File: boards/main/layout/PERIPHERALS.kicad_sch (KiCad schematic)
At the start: 42 parts, among them Q1 AO3400A, Q7 AO3401A, SW1 DSHP04TJGER, SW2 GT-TC048B-H025-L1, SW3 GT-TC048B-H025-L1, SW5 GT-TC048B-H025-L1, U2 GT-USB-7010ASV, U6 USBLC6-2SC6, U7 TLV7041DBVR

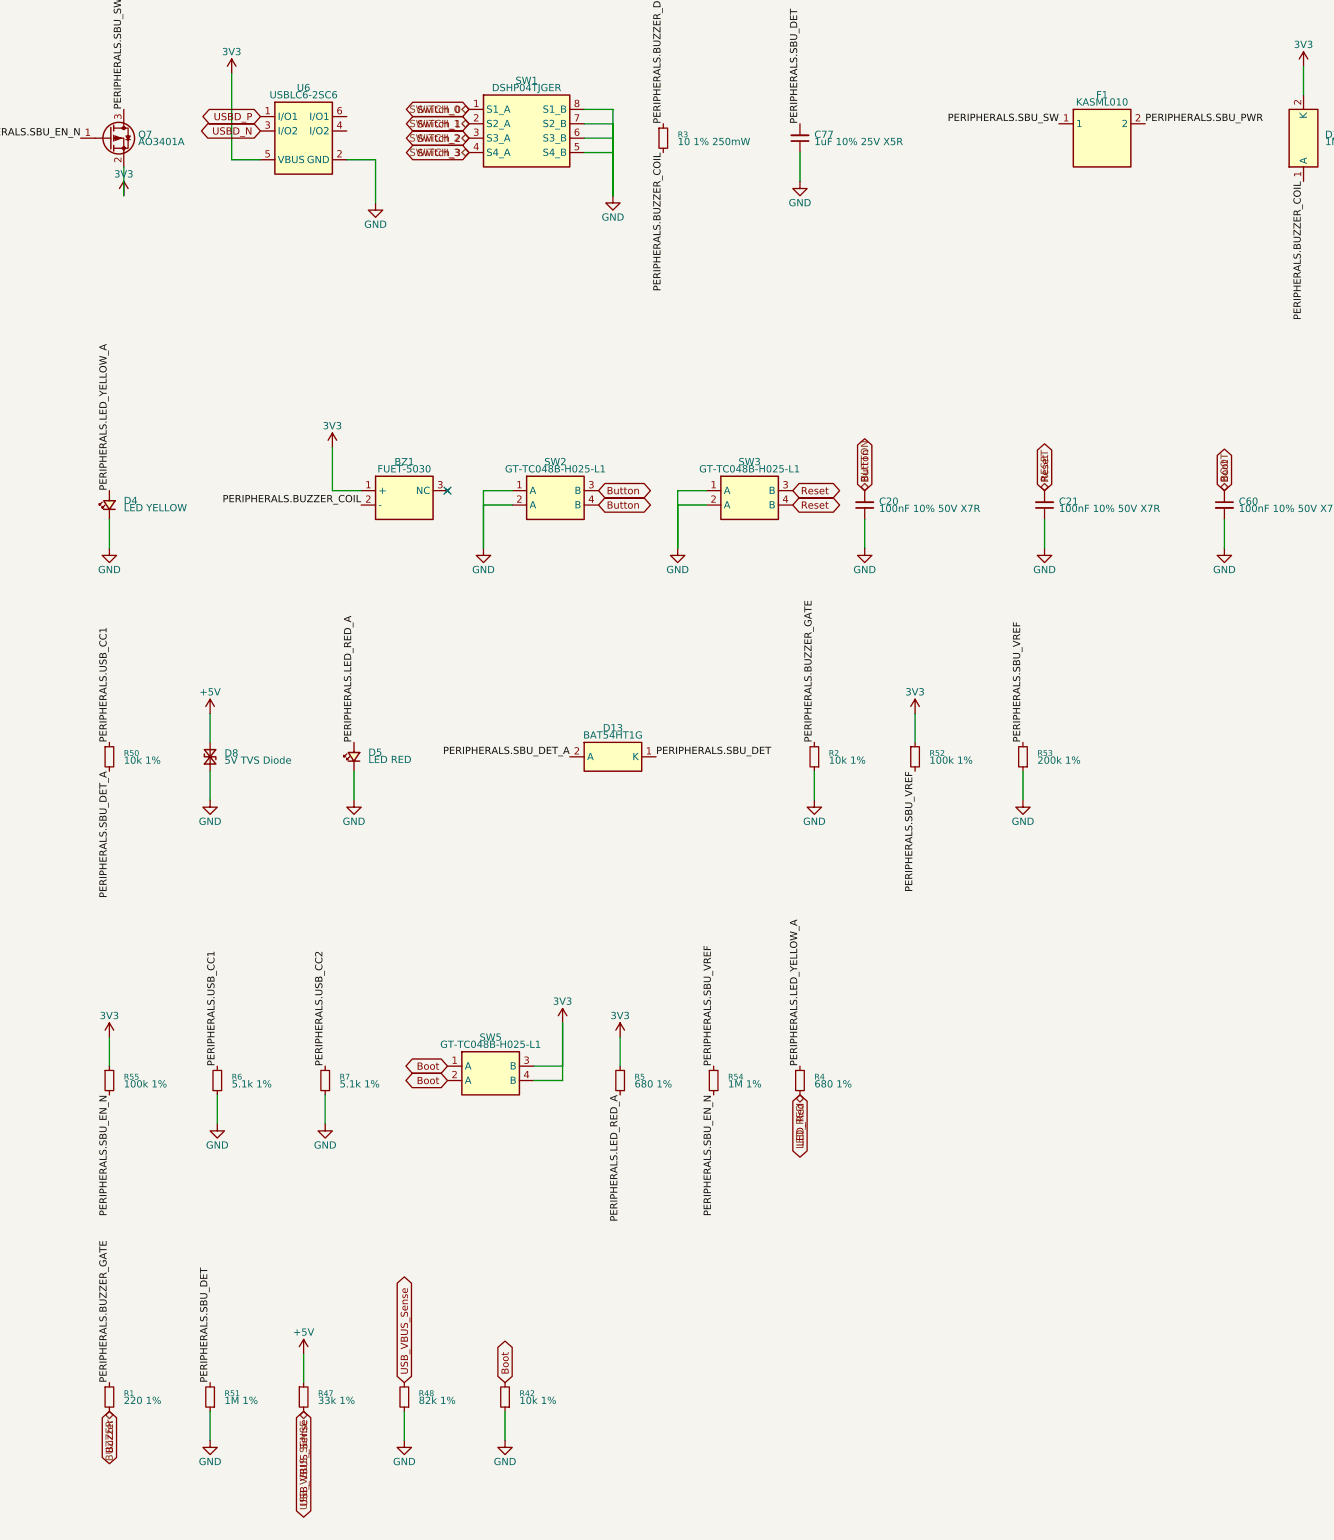
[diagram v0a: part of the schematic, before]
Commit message: 🏷️ Name the main board's module ports after their nets
A sheet pin and its hierarchical label take the module's port name and the root's label the net
name; KiCad's ERC flagged the 33 nets whose two names differed only in case (similar_labels).
GND_BAT becomes a ground port of REGULATORS, so the root shows a power symbol at its sheet pin
instead of a label nothing else joined (label_dangling).
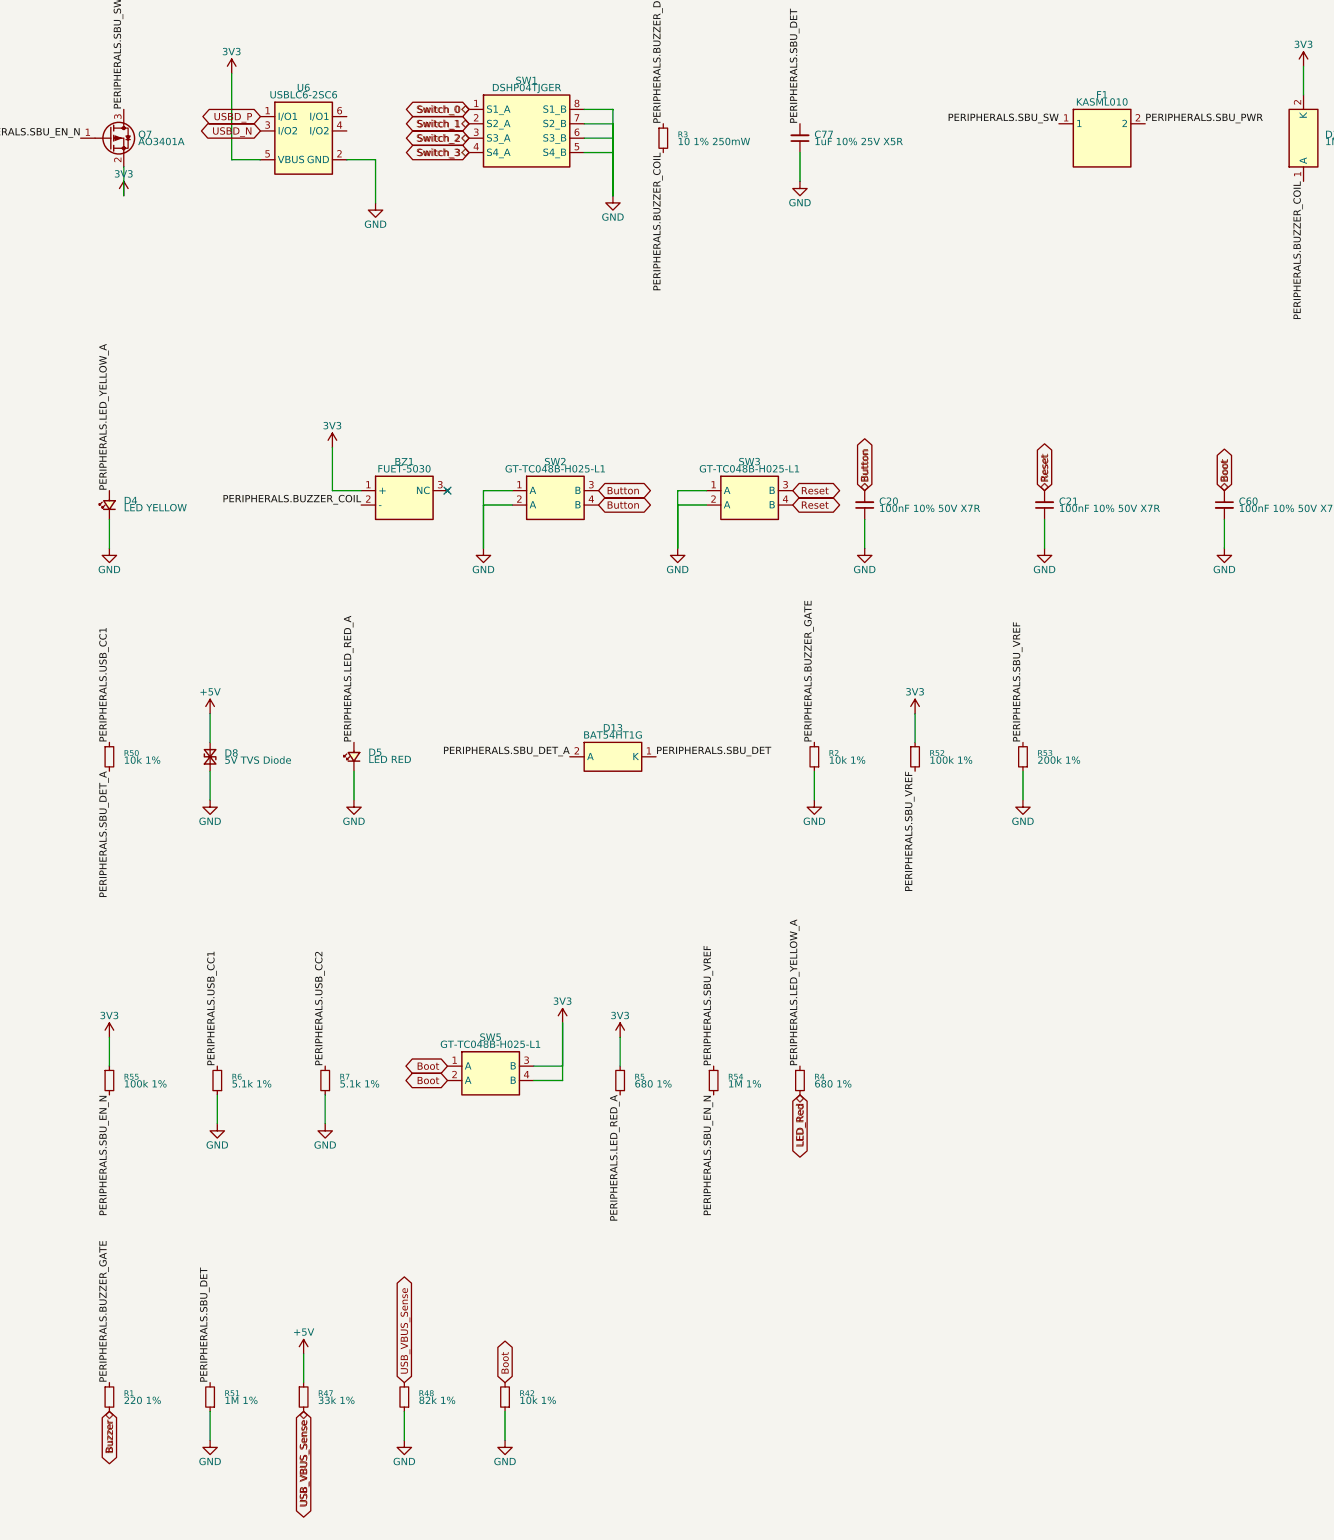
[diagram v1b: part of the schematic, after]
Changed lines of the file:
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@@
 		)
 	)
-	(hierarchical_label "SWITCH_0"
+	(hierarchical_label "USB_VBUS_Sense"
 		(shape bidirectional)
-		(at 181.61 132.08 180)
+		(at 152.4 361.95 270)
 		(effects
 			(font
@@
 		)
 	)
+	(hierarchical_label "Boot"
+		(shape bidirectional)
+		(at 314.96 199.39 90)
+		(effects
+			(font
+				(size 1.27 1.27)
+			)
+			(justify left)
+		)
+	)
+	(hierarchical_label "Switch_0"
+		(shape bidirectional)
+		(at 181.61 132.08 180)
+		(effects
+			(font
+				(size 1.27 1.27)
+			)
+			(justify right)
+		)
+	)
 	(hierarchical_label "LED_ARGB"
 		(shape bidirectional)
@@
 		)
 	)
-	(hierarchical_label "BOOT"
+	(hierarchical_label "Switch_2"
 		(shape bidirectional)
-		(at 314.96 199.39 90)
-		(effects
-			(font
-				(size 1.27 1.27)
-			)
-			(justify left)
-		)
-	)
-	(hierarchical_label "BUZZER"
-		(shape bidirectional)
-		(at 118.11 361.95 270)
+		(at 181.61 137.16 180)
 		(effects
 			(font
@@
 		)
 	)
-	(hierarchical_label "LED_RED"
+	(hierarchical_label "Switch_3"
 		(shape bidirectional)
-		(at 240.03 306.07 270)
+		(at 181.61 139.7 180)
 		(effects
 			(font
@@
 		)
 	)
-	(hierarchical_label "BUTTON"
+	(hierarchical_label "Reset"
 		(shape bidirectional)
-		(at 251.46 199.39 90)
+		(at 283.21 199.39 90)
 		(effects
 			(font
@@
 			)
 			(justify left)
-		)
-	)
-	(hierarchical_label "SWITCH_1"
-		(shape bidirectional)
-		(at 181.61 134.62 180)
-		(effects
-			(font
-				(size 1.27 1.27)
-			)
-			(justify right)
-		)
-	)
-	(hierarchical_label "SWITCH_3"
-		(shape bidirectional)
-		(at 181.61 139.7 180)
-		(effects
-			(font
-				(size 1.27 1.27)
-			)
-			(justify right)
 		)
 	)
@@
 		)
 	)
-	(hierarchical_label "USB_VBUS_SENSE"
+	(hierarchical_label "Button"
 		(shape bidirectional)
-		(at 152.4 361.95 270)
+		(at 251.46 199.39 90)
+		(effects
+			(font
+				(size 1.27 1.27)
+			)
+			(justify left)
+		)
+	)
+	(hierarchical_label "Buzzer"
+		(shape bidirectional)
+		(at 118.11 361.95 270)
 		(effects
 			(font
@@
 		)
 	)
-	(hierarchical_label "SWITCH_2"
+	(hierarchical_label "LED_Red"
 		(shape bidirectional)
-		(at 181.61 137.16 180)
+		(at 240.03 306.07 270)
 		(effects
 			(font
@@
 		)
 	)
-	(hierarchical_label "RESET"
+	(hierarchical_label "Switch_1"
 		(shape bidirectional)
-		(at 283.21 199.39 90)
+		(at 181.61 134.62 180)
 		(effects
 			(font
 				(size 1.27 1.27)
 			)
-			(justify left)
+			(justify right)
 		)
 	)

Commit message: 🎨 Place the main board's PERIPHERALS sheet; widen the USBLC6 symbol and draw the TLV7041's inputs as + and −
A wired pin of a jumper pin group (the USBLC6's second I/O pads) takes
the labels of its partners, so a wire from it carries the net's name.
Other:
- note added: "Addressable LEDs on VBAT"
- note added: "Bluetooth module supply on SBU: CC signature detector and switch"
- note added: "Buttons: user, reset, boot"
- note added: "Buzzer: low-side switch Q1, flyback D3"
- note added: "DIP switch"
- note added: "Indicator LEDs"
- note added: "Sheet ports"
- note added: "USB-C receptacle: VBUS sense, CC sink, ESD"
- title: (none) -> User interface and USB-C
- moved on the sheet: BZ1, C18, C19, C20, C21, C60, C77, C78, C79, D1, D13, D2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

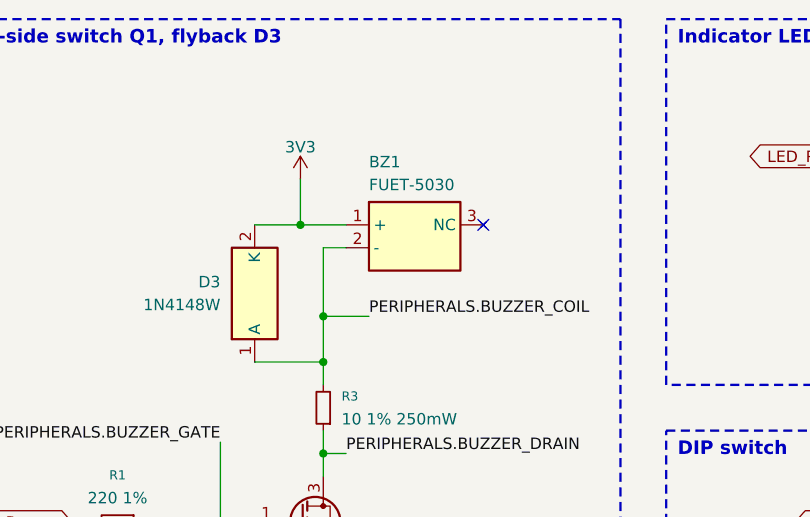
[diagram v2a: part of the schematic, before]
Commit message: 🎨 Draw the diodes and buzzer as symbols, and make D4 blue
- 1N4148WS, B5819W and FUET-5030: replace the box bodies with diode,
  Schottky and buzzer symbols (same pins). Nudge D3 and BZ1 on both boards'
  PERIPHERALS sheets.
- D4: KENTO KT-0603B blue (C2288, VF 2.6-3.1 V at 5 mA) instead of the
  yellow NCD0603Y2. R4 goes from 680 Ohm to 100 Ohm: 1.2 mA at the worst
  bin and rail, 7.5 mA at most. LED_YELLOW_A is renamed LED_BLUE_A.
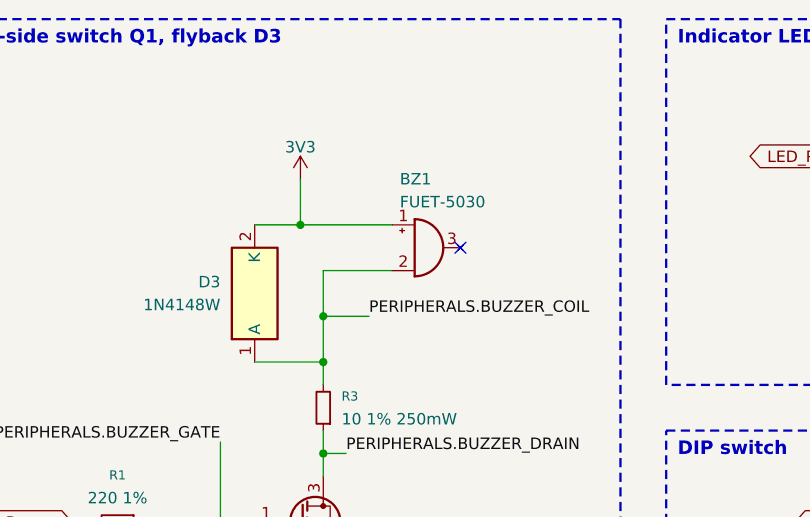
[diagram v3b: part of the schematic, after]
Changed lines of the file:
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@@
 		(dnp no)
 		(property "Reference" "BZ1"
-			(at 251.46 28.575 0)
+			(at 254.889 30.48 0)
 			(show_name no)
 			(do_not_autoplace no)
@@
 		)
 		(property "Value" "FUET-5030"
-			(at 251.46 31.115 0)
+			(at 254.889 33.02 0)
 			(show_name no)
 			(do_not_autoplace no)
@@
 	)
 	(no_connect
-		(at 264.16 35.56)
+		(at 261.62 38.1)
 	)
 	(no_connect
@@
 	(wire
 		(pts
-			(xy 243.84 35.56) (xy 248.92 35.56)
+			(xy 243.84 35.56) (xy 254 35.56)
 		)
 		(stroke
@@
 	(wire
 		(pts
-			(xy 248.92 38.1) (xy 246.38 38.1)
+			(xy 254 40.64) (xy 246.38 40.64)
 		)
 		(stroke
@@
 	(wire
 		(pts
-			(xy 246.38 38.1) (xy 246.38 45.72)
+			(xy 246.38 40.64) (xy 246.38 45.72)
 		)
 		(stroke
